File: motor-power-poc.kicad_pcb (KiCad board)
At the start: 4 copper layers, 149 parts, among them J1 Conn_01x04_Pin, J2 USB_C_Receptacle_USB2.0_14P, J3 Conn_01x02, J4 Conn_02x02_Counter_Clockwise, J5 Conn_02x06_Counter_Clockwise, M1 Motor_Servo, M2 Motor_Servo, M3 DC, Q1 Q_NMOS, Q10 Q_NMOS, Q2 Q_NMOS, Q3 Q_NMOS, Q4 Q_NMOS, Q5 Q_NMOS, Q6 Q_NMOS, Q7 Q_NMOS, Q8 Q_NMOS, Q9 Q_NMOS, SW1 SW_Push, SW2 SW_Push, U1 QRE1113GR, U10 CJ431, U11 DRV8701, U2 QRE1113GR, U3 QRE1113GR, U4 ESP32-S3FH4R2, U5 LM74502, U6 TPS5430DDA, U7 TPS56A37, U8 TPS2121, U9 LDL212PV33R, Y1 48M

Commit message: pcb: initial rough placement
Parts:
- moved U1 160.5 mm to (32.8, 161.4)
- moved U2 160.5 mm to (37.6, 161.4)
- moved U3 160.5 mm to (42.4, 161.4)
- moved C2 153.4 mm to (35.3, 165.7), turned to 90 degrees
- moved R1 151.6 mm to (31.5, 168.3), turned to 90 degrees
- moved C3 150.6 mm to (37.3, 165.7), turned to 90 degrees
- moved R2 148.1 mm to (34.0, 168.3), turned to 90 degrees
- moved C4 147.9 mm to (39.3, 165.7), turned to 90 degrees
- moved R3 144.6 mm to (36.5, 168.3), turned to 90 degrees
- moved R4 141.2 mm to (39.0, 168.3), turned to 90 degrees
- moved R5 137.7 mm to (41.5, 168.3), turned to 90 degrees
- moved R6 134.2 mm to (44.0, 168.3), turned to 90 degrees
- moved C27 125.1 mm to (31.0, 113.2)
- moved R13 120.9 mm to (53.6, 99.0)
- moved R14 120.9 mm to (53.6, 100.9)
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
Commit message: pcb: layout refinement
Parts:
- moved U7 159.7 mm to (197.0, 64.0), turned to 180 degrees
- moved R25 156.9 mm to (196.0, 59.8), turned to 180 degrees
- moved L7 156.4 mm to (193.9, 71.6), turned to 180 degrees
- moved D8 153.0 mm to (194.3, 57.1), turned to 180 degrees
- moved R18 148.9 mm to (191.4, 64.8), turned to 180 degrees
- moved R28 148.6 mm to (191.8, 61.1), turned to 180 degrees
- moved R20 148.4 mm to (191.8, 59.1), turned to 180 degrees
- moved R19 148.4 mm to (191.4, 62.8), turned to 180 degrees
- moved C29 141.6 mm to (188.0, 62.8), turned to 180 degrees
- moved C32 141.2 mm to (188.0, 60.8), turned to 180 degrees
- moved C33 140.8 mm to (188.0, 58.9), turned to 180 degrees
- moved C26 139.2 mm to (185.1, 71.3), turned to 180 degrees
- moved C28 137.7 mm to (185.1, 68.3), turned to 180 degrees
- moved C34 136.5 mm to (185.1, 65.3), turned to 180 degrees
- moved C35 135.6 mm to (185.1, 62.3), turned to 180 degrees
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
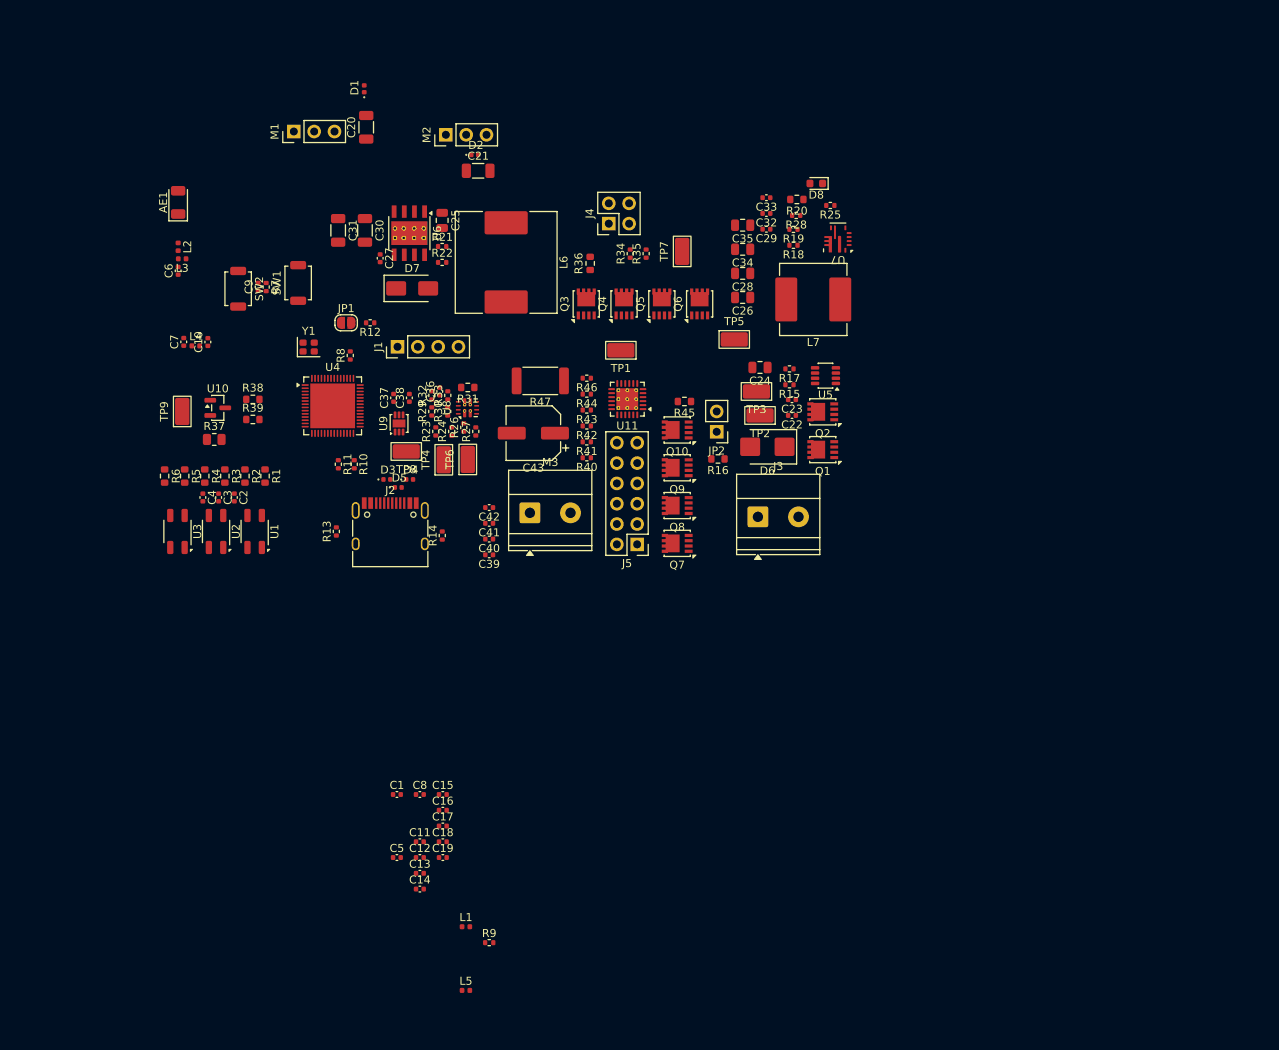
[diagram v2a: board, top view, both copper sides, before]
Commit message: pcb: add LM74502 RPP layout
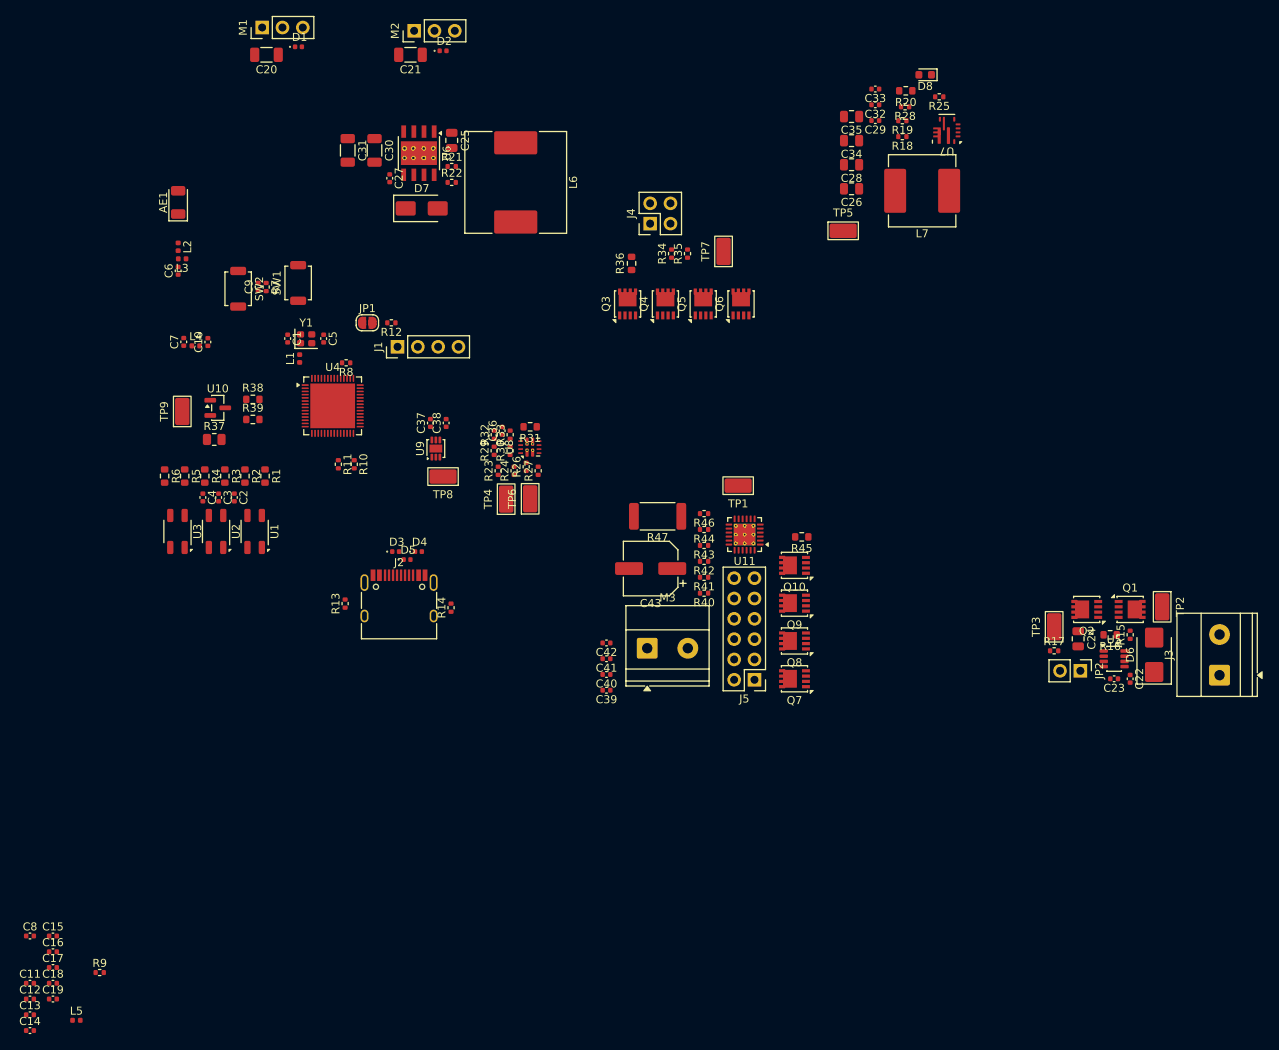
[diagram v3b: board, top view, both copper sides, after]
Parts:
- moved L1 74.0 mm to (129.7, 79.0), turned to 90 degrees
- moved C5 65.5 mm to (132.7, 76.5), turned to -90 degrees
- moved J3 61.0 mm to (244.7, 118.5), turned to 90 degrees
- moved C1 58.6 mm to (128.2, 76.5), turned to -90 degrees
- moved TP2 55.7 mm to (237.5, 110.0), turned to -90 degrees
- moved D6 54.9 mm to (236.5, 116.0), turned to 90 degrees
- moved JP2 54.4 mm to (227.3, 118.0), turned to -90 degrees
- moved R16 53.7 mm to (231.0, 113.5)
- moved C22 53.6 mm to (233.5, 119.0), turned to -90 degrees
- moved C23 53.3 mm to (231.5, 119.0)
- moved R15 52.8 mm to (233.5, 113.5), turned to 90 degrees
- moved C24 52.3 mm to (227.0, 114.0), turned to -90 degrees
- moved C15 51.8 mm to (98.8, 151.2)
- moved C16 51.8 mm to (98.8, 153.1)
- moved C17 51.8 mm to (98.8, 155.1)
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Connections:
- Q1 pad 1: /Connectors/EN/UVLO -> Net-(U5-SRC)
- Q1 pad 2: /Connectors/EN/UVLO -> Net-(U5-SRC)
- Q1 pad 3: /Connectors/EN/UVLO -> Net-(U5-SRC)
- Q1 pad 5: Net-(Q2-D) -> /Connectors/EN/UVLO
- Q10 pad 1: /H-bridge/+Vdc -> Net-(M3--)
- Q10 pad 2: /H-bridge/+Vdc -> Net-(M3--)
- Q10 pad 3: /H-bridge/+Vdc -> Net-(M3--)
- Q10 pad 5: Net-(M3--) -> /H-bridge/+Vdc
- Q2 pad 1: +Vin -> Net-(U5-SRC)
- Q2 pad 2: +Vin -> Net-(U5-SRC)
- Q2 pad 3: +Vin -> Net-(U5-SRC)
- Q2 pad 5: Net-(Q2-D) -> +Vin
- Q3 pad 1: +12V -> Net-(Q3-S-Pad1)
- Q3 pad 2: +12V -> Net-(Q3-S-Pad1)
- Q3 pad 3: +12V -> Net-(Q3-S-Pad1)
- Q3 pad 5: Net-(Q3-D) -> +12V
- Q4 pad 1: /H-bridge/+Vdc -> Net-(Q3-S-Pad1)
- Q4 pad 2: /H-bridge/+Vdc -> Net-(Q3-S-Pad1)
- Q4 pad 3: /H-bridge/+Vdc -> Net-(Q3-S-Pad1)
- Q4 pad 5: Net-(Q3-D) -> /H-bridge/+Vdc
- Q5 pad 1: /H-bridge/+Vdc -> Net-(Q5-S-Pad1)
- Q5 pad 2: /H-bridge/+Vdc -> Net-(Q5-S-Pad1)
- Q5 pad 3: /H-bridge/+Vdc -> Net-(Q5-S-Pad1)
- Q5 pad 5: Net-(Q5-D) -> /H-bridge/+Vdc
- Q6 pad 1: +Vin -> Net-(Q5-S-Pad1)
- Q6 pad 2: +Vin -> Net-(Q5-S-Pad1)
- Q6 pad 3: +Vin -> Net-(Q5-S-Pad1)
- Q6 pad 5: Net-(Q5-D) -> +Vin
- Q7 pad 1: /H-bridge/+Vdc -> Net-(M3-+)
- Q7 pad 2: /H-bridge/+Vdc -> Net-(M3-+)
- Q7 pad 3: /H-bridge/+Vdc -> Net-(M3-+)
- Q7 pad 5: Net-(M3-+) -> /H-bridge/+Vdc
- Q8 pad 1: Net-(M3-+) -> Net-(U11-SP)
- Q8 pad 2: Net-(M3-+) -> Net-(U11-SP)
- Q8 pad 3: Net-(M3-+) -> Net-(U11-SP)
- Q8 pad 5: Net-(Q9-D) -> Net-(M3-+)
- Q9 pad 1: Net-(M3--) -> Net-(U11-SP)
- Q9 pad 2: Net-(M3--) -> Net-(U11-SP)
- Q9 pad 3: Net-(M3--) -> Net-(U11-SP)
- Q9 pad 5: Net-(Q9-D) -> Net-(M3--)
- R47 pad 1: Net-(Q9-D) -> Net-(U11-SP)
- U11 pad 21: Net-(Q9-D) -> Net-(U11-SP)
- U5 pad 8: Net-(Q2-D) -> Net-(U5-SRC)

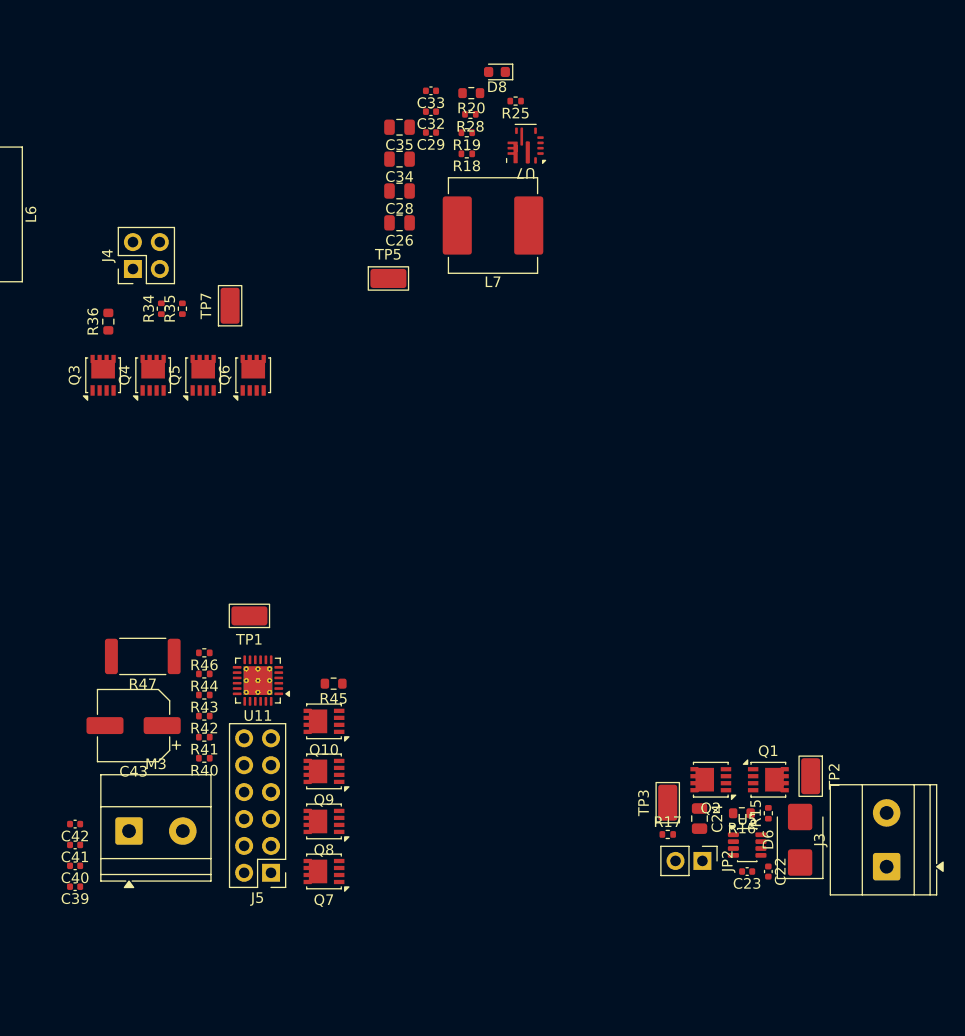
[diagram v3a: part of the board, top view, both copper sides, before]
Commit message: pcb: add TPS56A37 layout
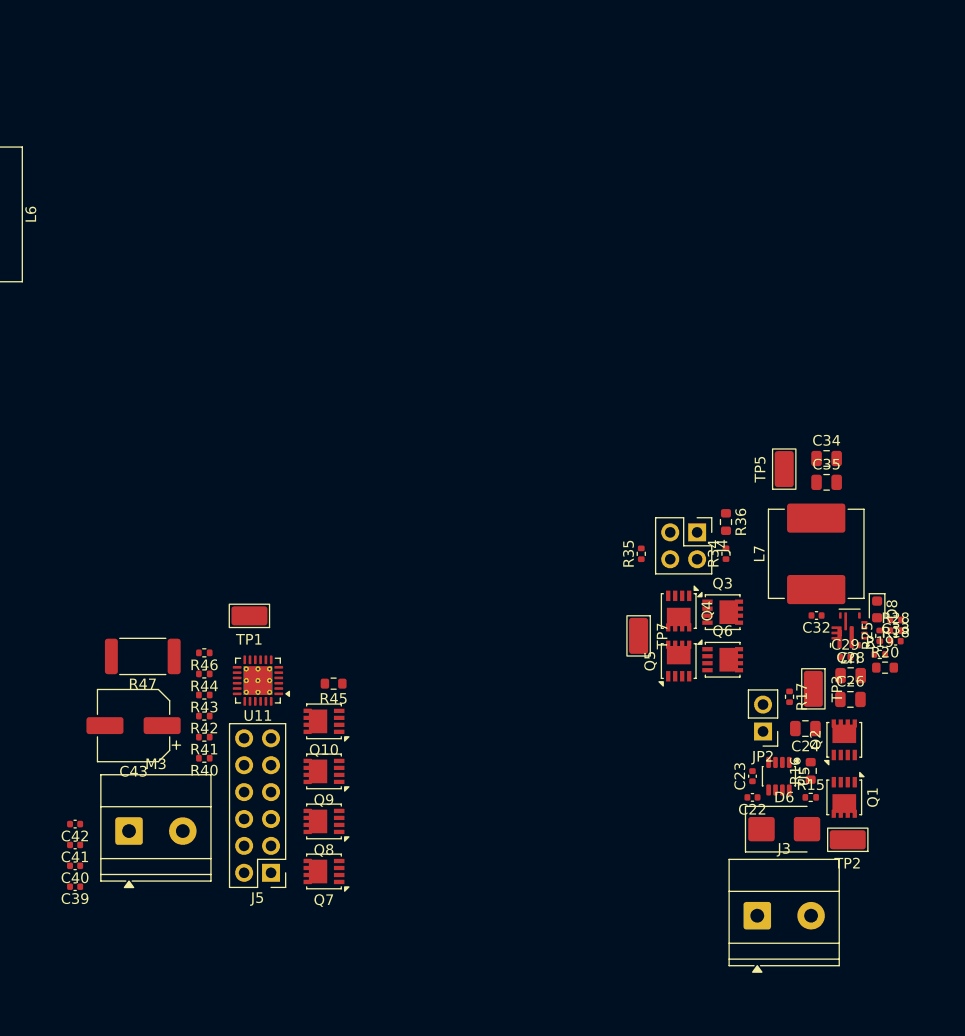
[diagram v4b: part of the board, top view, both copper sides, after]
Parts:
- moved C33 68.0 mm to (245.5, 97.2), turned to 0 degrees
- moved R20 66.9 mm to (244.5, 99.8), turned to 0 degrees
- moved R28 63.2 mm to (245.5, 96.2), turned to 0 degrees
- moved C29 63.1 mm to (240.8, 98.8), turned to 0 degrees
- moved R19 62.8 mm to (244.0, 98.5), turned to 0 degrees
- moved Q3 62.6 mm to (229.2, 94.5), turned to 0 degrees
- moved C28 62.5 mm to (241.3, 100.5), turned to 0 degrees
- moved D8 62.2 mm to (243.8, 94.2), turned to -90 degrees
- moved C26 61.9 mm to (241.2, 102.8), turned to 0 degrees
- moved R36 61.3 mm to (229.5, 86.0), turned to -90 degrees
- moved R25 61.1 mm to (244.0, 96.8), turned to 90 degrees
- moved C32 59.9 mm to (238.1, 94.8)
- moved R18 59.8 mm to (245.5, 95.2)
- moved J4 58.8 mm to (226.8, 87.0), turned to -90 degrees
- moved R34 58.1 mm to (229.5, 89.0)
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
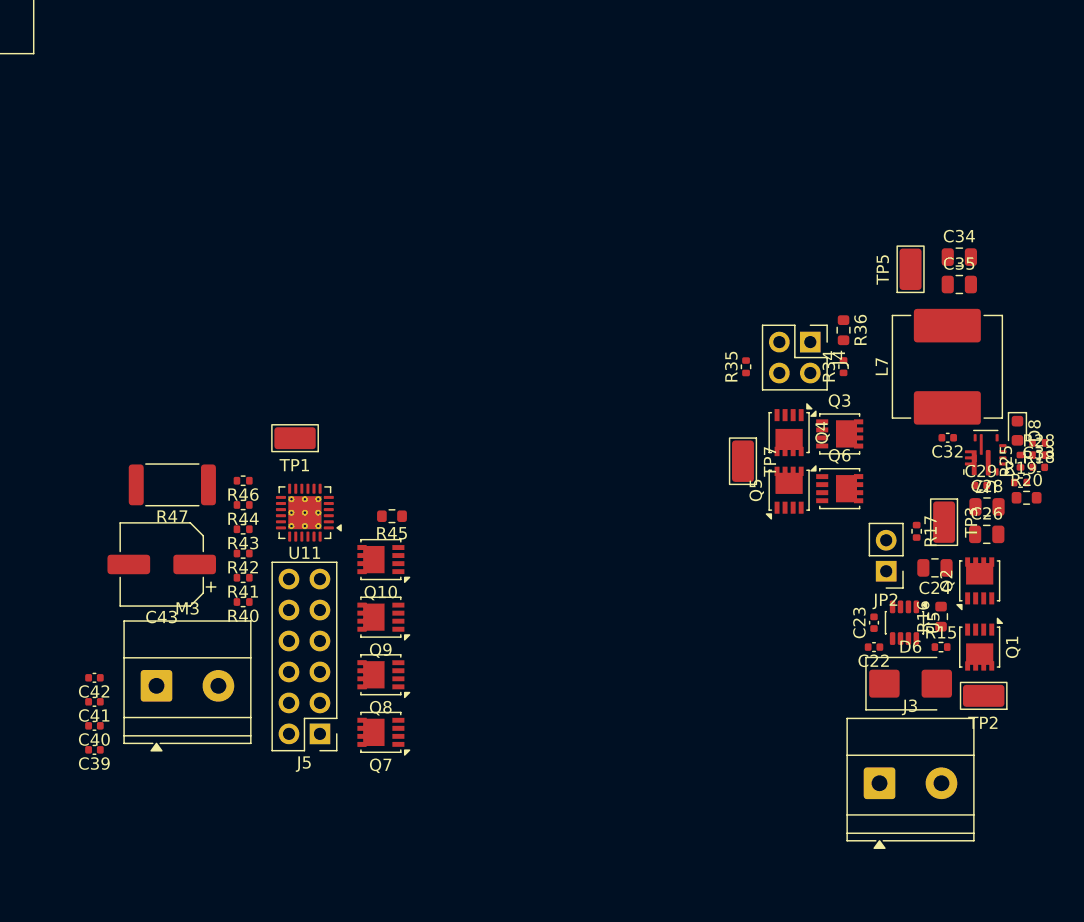
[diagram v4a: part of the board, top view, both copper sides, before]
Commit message: pcb: add DRV8701 layout
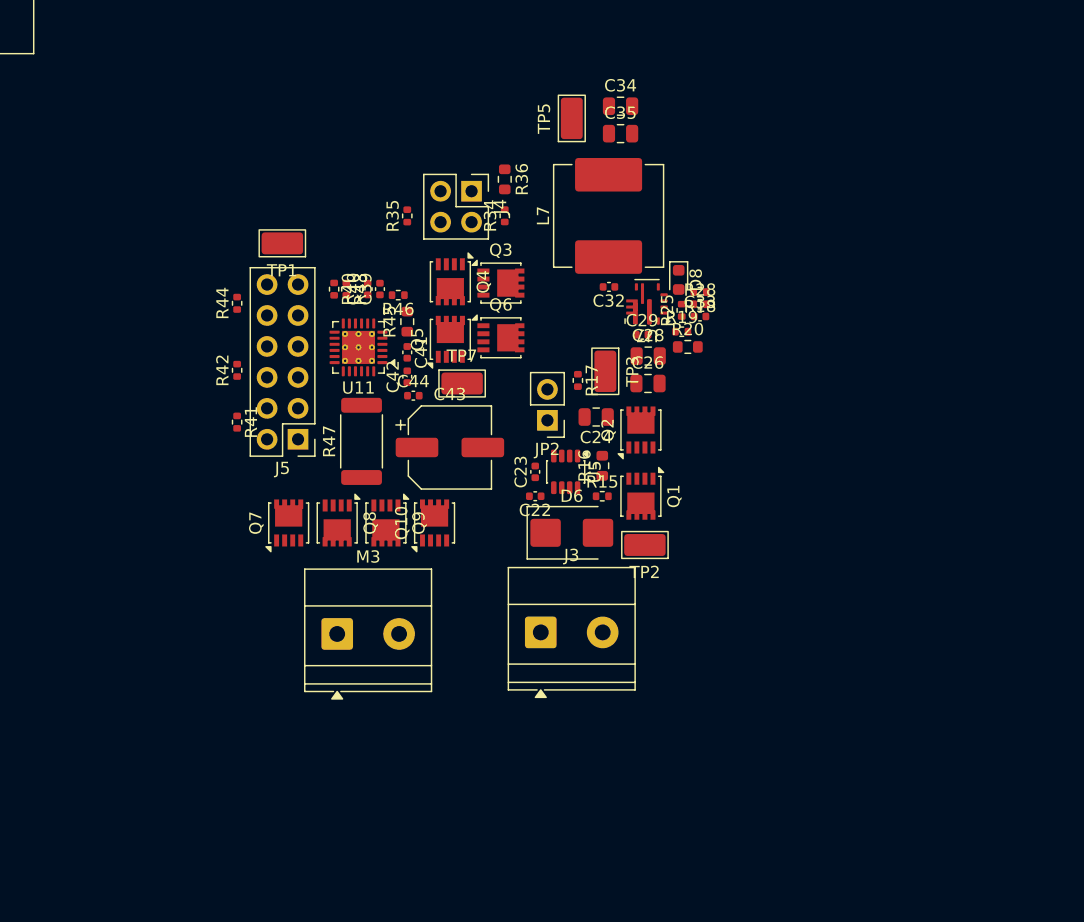
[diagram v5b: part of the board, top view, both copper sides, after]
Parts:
- added C44: 0u1, Capacitor_SMD:C_0402_1005Metric, F.Cu at (194.2, 91.4)
- moved C39 44.5 mm to (191.5, 82.6), turned to 90 degrees
- moved C40 42.3 mm to (190.5, 82.6), turned to 90 degrees
- moved C41 38.5 mm to (193.7, 87.8), turned to -90 degrees
- moved C42 35.6 mm to (193.7, 89.8), turned to 90 degrees
- moved Q3 30.4 mm to (201.4, 82.1)
- moved C28 30.4 mm to (213.5, 88.1)
- moved C29 30.4 mm to (213.0, 86.4)
- moved C32 30.4 mm to (210.3, 82.4)
- moved C33 30.4 mm to (217.7, 84.9)
- moved D8 30.4 mm to (216.0, 81.9)
- moved J3 30.4 mm to (204.7, 110.8)
- moved J4 30.4 mm to (199.0, 74.6)
- moved L7 30.4 mm to (210.2, 76.6)
- moved Q6 30.4 mm to (201.4, 86.6)
- moved R18 30.4 mm to (217.7, 82.9)
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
